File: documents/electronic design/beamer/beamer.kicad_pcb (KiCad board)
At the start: 2 copper layers, 23 parts, among them P1 CONN_01X20, P2 CONN_01X20, T1 2N7002K, T10 2N7002K, T2 2N7002K, T3 2N7002K, T4 2N7002K, T5 2N7002K, T6 2N7002K, T7 2N7002K, T8 2N7002K, T9 2N7002K, U1 NRF24L01-BRKOUT

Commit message: update pcb
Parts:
- moved U1 97.5 mm to (224.5, 110.7), turned to 270 degrees
- moved R1 91.4 mm to (172.7, 109.2), turned to 90 degrees
- moved P1 71.7 mm to (193.0, 124.5)
- moved P2 71.7 mm to (193.0, 109.2)
- moved D4 58.6 mm to (90.0, 110.1)
- moved D5 58.6 mm to (105.0, 110.1)
- moved D6 58.6 mm to (120.0, 110.1)
- moved D7 58.6 mm to (135.0, 110.1)
- moved D8 58.6 mm to (150.0, 110.1)
- moved D9 58.6 mm to (165.0, 110.1)
- moved D1 58.6 mm to (45.0, 110.1)
- moved D2 58.6 mm to (60.0, 110.1)
- moved D3 58.6 mm to (75.0, 110.1)
- moved T10 50.1 mm to (163.7, 114.3)
- moved T8 50.1 mm to (133.7, 114.3)
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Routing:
- net Net-(D1-Pad1): track 125.6 -> 4.52 mm
- net Net-(D2-Pad1): track 101.0 -> 4.52 mm
- net Net-(D5-Pad1): track 94.8 -> 4.52 mm
- net Net-(D4-Pad1): track 86.1 -> 4.52 mm
- net Net-(D3-Pad1): track 83.8 -> 4.52 mm
- net PWM_38K: track 74.3 -> 0.00 mm
- net IR_PIN_1: track 64.4 -> 0.00 mm
- net IR_PIN_ID: track 58.1 -> 0.00 mm
- net IR_PIN_2: track 51.4 -> 0.00 mm
- net IR_PIN_8: track 46.4 -> 0.00 mm
- net IR_PIN_3: track 38.5 -> 0.00 mm
- net GND: track 0.00 -> 37.1 mm
- net IR_PIN_7: track 34.0 -> 0.00 mm
- net +3V3: track 0.00 -> 31.6 mm
- net IR_PIN_4: track 27.7 -> 0.00 mm
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
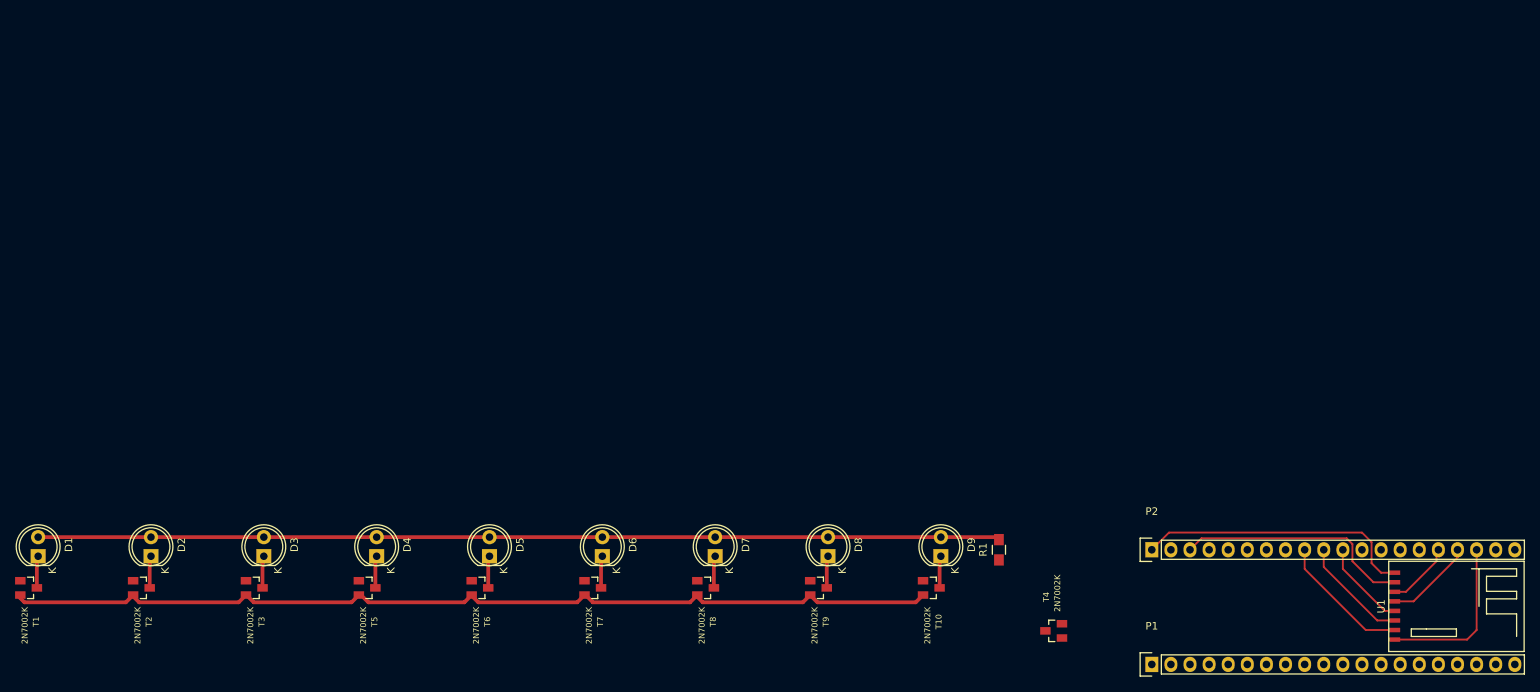
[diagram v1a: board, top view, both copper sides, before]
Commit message: finish pcb for beamer (prototype v1)
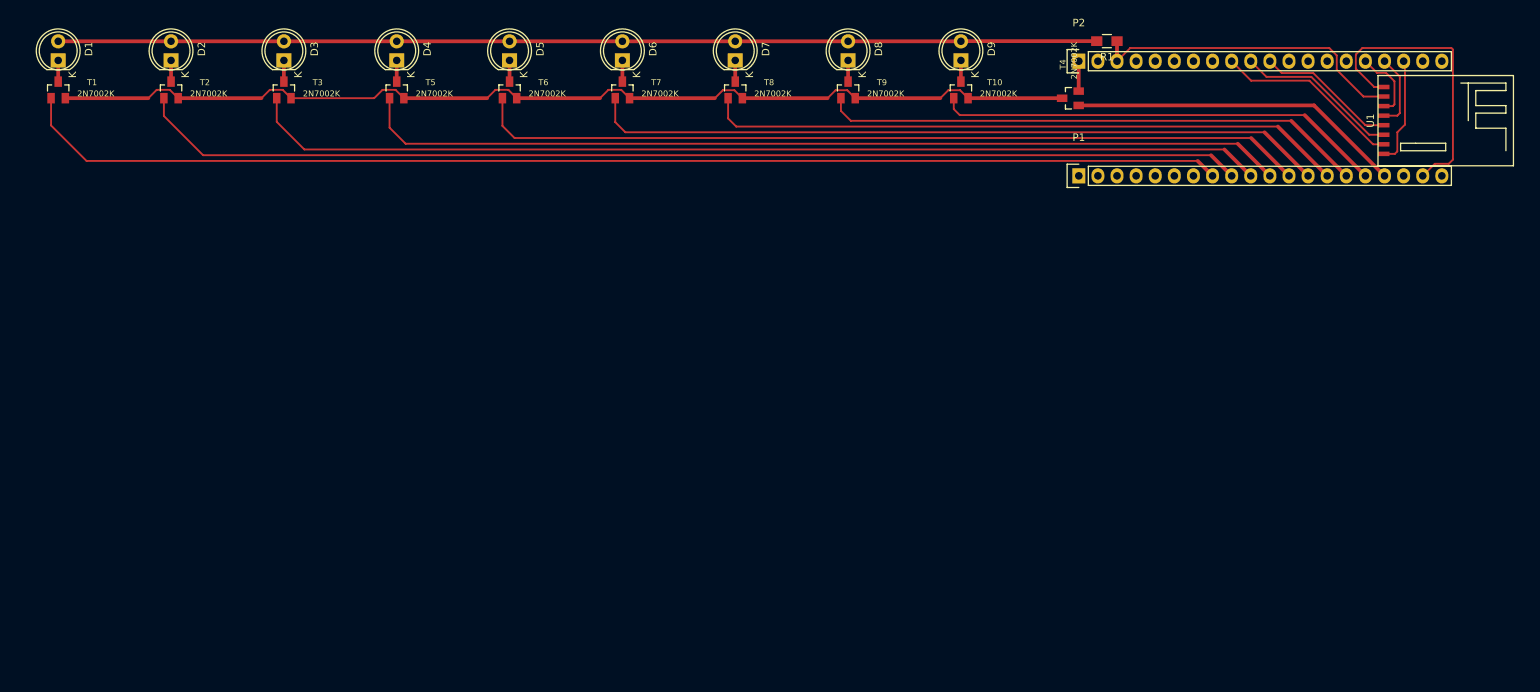
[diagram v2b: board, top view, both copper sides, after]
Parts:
- moved T4 70.8 mm to (182.2, 49.2)
- moved R1 69.1 mm to (187.1, 41.6), turned to 180 degrees
- moved T10 66.3 mm to (167.7, 48.1), turned to 0 degrees
- moved T8 66.3 mm to (137.7, 48.1), turned to 0 degrees
- moved T9 66.3 mm to (152.7, 48.1), turned to 0 degrees
- moved T1 66.3 mm to (47.7, 48.1), turned to 0 degrees
- moved T2 66.3 mm to (62.7, 48.1), turned to 0 degrees
- moved T3 66.3 mm to (77.7, 48.1), turned to 0 degrees
- moved T5 66.3 mm to (92.7, 48.1), turned to 0 degrees
- moved T6 66.3 mm to (107.7, 48.1), turned to 0 degrees
- moved T7 66.3 mm to (122.7, 48.1), turned to 0 degrees
- moved D1 66.0 mm to (47.7, 44.2)
- moved D2 66.0 mm to (62.7, 44.2)
- moved D3 66.0 mm to (77.7, 44.2)
- moved D4 66.0 mm to (92.7, 44.2)
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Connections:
- P1 pad 19: Net-(P1-Pad19) -> GND
- P1 pad 20: Net-(P1-Pad20) -> +3V3
- P2 pad 2: Net-(P2-Pad2) -> GND
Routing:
- net IR_PIN_1: track 0.00 -> 160.8 mm
- net IR_PIN_2: track 0.00 -> 147.6 mm
- net IR_PIN_3: track 0.00 -> 135.6 mm
- net IR_PIN_4: track 0.00 -> 123.6 mm
- net IR_PIN_5: track 0.00 -> 111.0 mm
- net IR_PIN_6: track 0.00 -> 98.2 mm
- net IR_PIN_7: track 0.00 -> 85.5 mm
- net IR_PIN_8: track 0.00 -> 72.4 mm
- net IR_PIN_ID: track 0.00 -> 59.8 mm
- net PWM_38K: track 0.00 -> 44.5 mm
- net Net-(T1-Pad2): track 127.0 -> 139.7 mm
- net +3V3: track 31.6 -> 42.7 mm
- net Net-(D1-Pad2): track 127.9 -> 138.1 mm
- net NRF_IRQ1: track 22.1 -> 14.4 mm
- net SPI1_MOSI: track 14.6 -> 21.7 mm
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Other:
- net class Default: trace_width 0.25 -> 0.5

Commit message: thick traces
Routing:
- net GND: track 43.5 -> 78.6 mm
- net IR_PIN_2: track 147.6 -> 158.9 mm
- net IR_PIN_3: track 135.6 -> 143.9 mm
- net +3V3: track 42.7 -> 50.2 mm
- net IR_PIN_1: track 160.8 -> 167.5 mm
- net IR_PIN_4: track 123.6 -> 126.6 mm
- net IR_PIN_5: track 111.0 -> 113.3 mm
- net IR_PIN_6: track 98.2 -> 100.1 mm
- net IR_PIN_8: track 72.4 -> 74.3 mm
- net IR_PIN_7: track 85.5 -> 87.0 mm
- net IR_PIN_ID: track 59.8 -> 61.0 mm

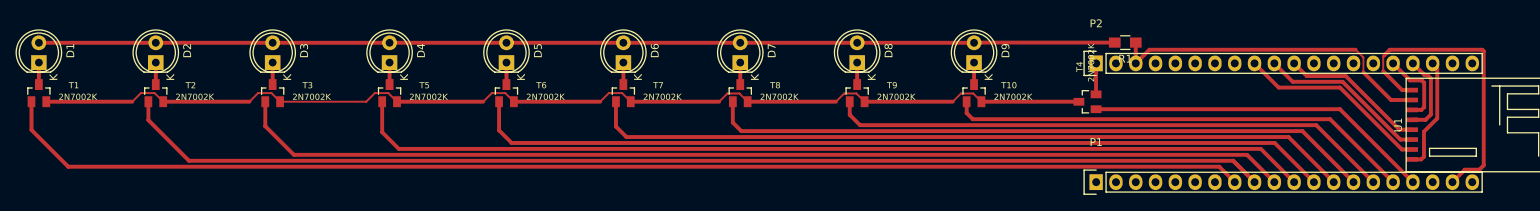
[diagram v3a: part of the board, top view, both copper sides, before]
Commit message: change pin numbers in transmitter routine; remake pcb
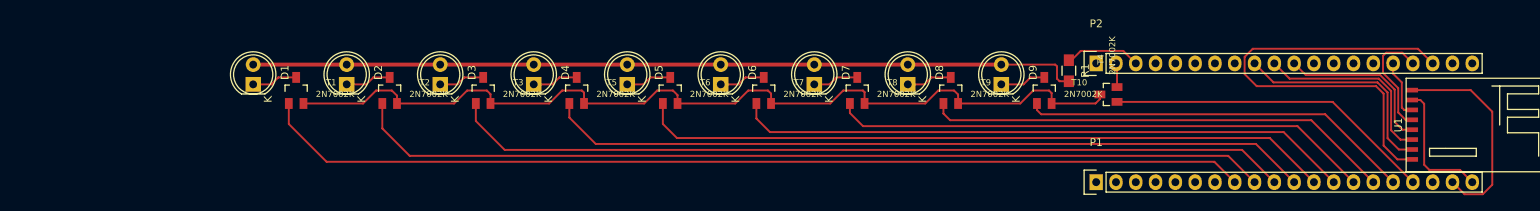
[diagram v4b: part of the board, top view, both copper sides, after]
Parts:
- T1, T10, T2, T3, T5, T6, T7, T8, T9: footprint 2N7002K:SOT23 -> sot23_modified:SOT23Mod
- moved T1 33.0 mm to (80.7, 47.7)
- moved T2 30.0 mm to (92.7, 47.7)
- moved D1 27.6 mm to (75.2, 47.0)
- moved T3 27.0 mm to (104.7, 47.7)
- moved D2 24.7 mm to (87.2, 47.0)
- moved T5 24.0 mm to (116.7, 47.7)
- moved D3 21.7 mm to (99.2, 47.0)
- moved T6 21.0 mm to (128.7, 47.7)
- moved D4 18.7 mm to (111.2, 47.0)
- moved T7 18.0 mm to (140.7, 47.7)
- moved D5 15.7 mm to (123.2, 47.0)
- moved T8 15.0 mm to (152.7, 47.7)
- moved D6 12.8 mm to (135.2, 47.0)
- moved T9 12.0 mm to (164.7, 47.7)
- moved D7 9.90 mm to (147.2, 47.0)
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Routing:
- net GND: track 78.6 -> 30.6 mm
- net NRF_IRQ1: track 14.8 -> 57.7 mm
- net IR_PIN_2: track 158.9 -> 118.0 mm
- net IR_PIN_1: track 167.5 -> 127.1 mm
- net IR_PIN_3: track 143.9 -> 108.0 mm
- net Net-(D1-Pad2): track 138.1 -> 107.7 mm
- net IR_PIN_4: track 126.6 -> 98.2 mm
- net IR_PIN_5: track 113.3 -> 89.3 mm
- net +3V3: track 50.2 -> 27.1 mm
- net IR_PIN_6: track 100.1 -> 79.4 mm
- net Net-(T1-Pad2): track 139.7 -> 119.8 mm
- net IR_PIN_7: track 87.0 -> 69.5 mm
- net IR_PIN_8: track 74.3 -> 60.1 mm
- net IR_PIN_ID: track 61.0 -> 50.4 mm
- net NRF_CSN1: track 10.4 -> 14.8 mm
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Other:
- net class Default: trace_width 0.5 -> 0.25

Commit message: add capacitor to pcb
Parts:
- added C1: C, Capacitors_SMD:C_1210_HandSoldering, F.Cu at (237.5, 44.2)
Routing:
- net +3V3: track 27.1 -> 61.3 mm
- net GND: track 30.6 -> 48.9 mm
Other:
- net class Default: trace_width 0.25 -> 0.5
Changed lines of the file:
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@@
 (kicad_pcb (version 4) (host pcbnew 4.0.2-stable)
   (general
-    (links 50)
+    (links 52)
     (no_connects 8)
-    (area 15.8222 13.9172 278.230001 189.330001)
+    (area 14.6792 16.7112 276.960001 190.3522)
     (thickness 1.6)
     (drawings 0)
-    (tracks 182)
+    (tracks 196)
     (zones 0)
-    (modules 23)
+    (modules 24)
     (nets 49)
   )
@@
     (35 F.Paste user)
     (36 B.SilkS user)
-    (37 F.SilkS user hide)
+    (37 F.SilkS user)
     (38 B.Mask user)
     (39 F.Mask user)
@@
   )
   (setup
-    (last_trace_width 0.25)
+    (last_trace_width 0.5)
     (trace_clearance 0.2)
     (zone_clearance 0.508)
@@
   (net_class Default "This is the default net class."
     (clearance 0.2)
-    (trace_width 0.25)
+    (trace_width 0.5)
     (via_dia 0.6)
     (via_drill 0.4)
@@
     (pad 3 smd rect (at 0.00254 -1.64338) (size 1 1.4) (layers F.Cu F.Paste F.Mask)
       (net 10 "Net-(D9-Pad1)") (solder_mask_margin 0.2))
+  )
+  (module Capacitors_SMD:C_1210_HandSoldering (layer F.Cu)
+    (at 237.49 44.196)
+    (descr "Capacitor SMD 1210, hand soldering")
+    (tags "capacitor 1210")
+    (attr smd)
+    (fp_text reference C1 (at 0 -2.7) (layer F.SilkS)
+      (effects (font (size 1 1) (thickness 0.15)))
+    )
+    (fp_text value C (at 0 2.7) (layer F.Fab)
+      (effects (font (size 1 1) (thickness 0.15)))
+    )
+    (fp_line (start -3.3 -1.6) (end 3.3 -1.6) (layer F.CrtYd) (width 0.05))
+    (fp_line (start -3.3 1.6) (end 3.3 1.6) (layer F.CrtYd) (width 0.05))
+    (fp_line (start -3.3 -1.6) (end -3.3 1.6) (layer F.CrtYd) (width 0.05))
+    (fp_line (start 3.3 -1.6) (end 3.3 1.6) (layer F.CrtYd) (width 0.05))
+    (fp_line (start 1 -1.475) (end -1 -1.475) (layer F.SilkS) (width 0.15))
+    (fp_line (start -1 1.475) (end 1 1.475) (layer F.SilkS) (width 0.15))
+    (pad 1 smd rect (at -2 0) (size 2 2.5) (layers F.Cu F.Paste F.Mask)
+      (net 26 GND))
+    (pad 2 smd rect (at 2 0) (size 2 2.5) (layers F.Cu F.Paste F.Mask)
+      (net 27 +3V3))
+    (model Capacitors_SMD.3dshapes/C_1210_HandSoldering.wrl
+      (at (xyz 0 0 0))
+      (scale (xyz 1 1 1))
+      (rotate (xyz 0 0 0))
+    )
   )
   (segment (start 75.1638 46.9652) (end 77.4948 46.9652) (width 0.25) (layer F.Cu) (net 1))
@@
   (segment (start 186.012 49.21) (end 213.675 49.21) (width 0.25) (layer F.Cu) (net 24))
   (segment (start 213.675 49.21) (end 223.9772 59.5122) (width 0.25) (layer F.Cu) (net 24))
+  (segment (start 235.49 44.196) (end 234.8992 44.196) (width 0.5) (layer F.Cu) (net 26))
+  (segment (start 234.8992 44.196) (end 231.394 47.7012) (width 0.5) (layer F.Cu) (net 26))
+  (segment (start 223.8756 47.7012) (end 231.394 47.7012) (width 0.5) (layer F.Cu) (net 26))
+  (segment (start 231.394 47.7012) (end 233.68 49.9872) (width 0.5) (layer F.Cu) (net 26))
+  (segment (start 233.68 49.9872) (end 233.68 57.15) (width 0.5) (layer F.Cu) (net 26))
+  (segment (start 233.68 57.15) (end 232.918 57.912) (width 0.5) (layer F.Cu) (net 26))
+  (segment (start 232.918 57.912) (end 230.378 57.912) (width 0.5) (layer F.Cu) (net 26))
+  (segment (start 230.378 57.912) (end 229.0572 59.2328) (width 0.5) (layer F.Cu) (net 26))
+  (segment (start 229.0572 59.2328) (end 229.0572 59.5122) (width 0.5) (layer F.Cu) (net 26))
+  (segment (start 229.0572 59.5122) (end 229.0572 59.2328) (width 0.25) (layer F.Cu) (net 26))
+  (segment (start 229.0572 59.2328) (end 230.378 57.912) (width 0.25) (layer F.Cu) (net 26))
+  (segment (start 230.378 57.912) (end 232.918 57.912) (width 0.25) (layer F.Cu) (net 26))
+  (segment (start 232.918 57.912) (end 233.68 57.15) (width 0.25) (layer F.Cu) (net 26))
+  (segment (start 233.68 57.15) (end 233.68 49.9872) (width 0.25) (layer F.Cu) (net 26))
+  (segment (start 233.68 49.9872) (end 231.394 47.7012) (width 0.25) (layer F.Cu) (net 26))
   (segment (start 186.012 47.31) (end 186.012 44.407) (width 0.25) (layer F.Cu) (net 26))
   (segment (start 186.012 44.407) (end 185.8772 44.2722) (width 0.25) (layer F.Cu) (net 26))
   (segment (start 183.0148 44.5946) (end 183.3372 44.2722) (width 0.25) (layer F.Cu) (net 26))
-  (segment (start 223.8756 47.7012) (end 231.394 47.7012) (width 0.25) (layer F.Cu) (net 26))
-  (segment (start 230.6066 61.0616) (end 229.0572 59.5122) (width 0.25) (layer F.Cu) (net 26))
-  (segment (start 232.9434 61.0616) (end 230.6066 61.0616) (width 0.25) (layer F.Cu) (net 26))
-  (segment (start 234.1626 59.8424) (end 232.9434 61.0616) (width 0.25) (layer F.Cu) (net 26))
-  (segment (start 234.1626 50.4698) (end 234.1626 59.8424) (width 0.25) (layer F.Cu) (net 26))
-  (segment (start 231.394 47.7012) (end 234.1626 50.4698) (width 0.25) (layer F.Cu) (net 26))
+  (segment (start 239.49 44.196) (end 239.49 59.0362) (width 0.5) (layer F.Cu) (net 27))
+  (segment (start 239.49 59.0362) (end 239.014 59.5122) (width 0.5) (layer F.Cu) (net 27))
+  (segment (start 239.014 59.5122) (end 231.5972 59.5122) (width 0.5) (layer F.Cu) (net 27))
+  (segment (start 239.014 59.5122) (end 231.5972 59.5122) (width 0.25) (layer F.Cu) (net 27))
+  (segment (start 239.49 59.0362) (end 239.014 59.5122) (width 0.25) (layer F.Cu) (net 27))
+  (segment (start 223.8756 48.9712) (end 224.9932 48.9712) (width 0.25) (layer F.Cu) (net 27))
+  (segment (start 230.0732 61.0362) (end 231.5972 59.5122) (width 0.25) (layer F.Cu) (net 27))
+  (segment (start 225.933 61.0362) (end 230.0732 61.0362) (width 0.25) (layer F.Cu) (net 27))
+  (segment (start 225.2472 60.3504) (end 225.933 61.0362) (width 0.25) (layer F.Cu) (net 27))
+  (segment (start 225.2472 49.2252) (end 225.2472 60.3504) (width 0.25) (layer F.Cu) (net 27))
+  (segment (start 224.9932 48.9712) (end 225.2472 49.2252) (width 0.25) (layer F.Cu) (net 27))
   (segment (start 179.832 43.862) (end 180.166 43.862) (width 0.25) (layer F.Cu) (net 27))
   (segment (start 180.166 43.862) (end 181.356 42.672) (width 0.25) (layer F.Cu) (net 27))
   (segment (start 181.356 42.672) (end 186.817 42.672) (width 0.25) (layer F.Cu) (net 27))
   (segment (start 186.817 42.672) (end 188.4172 44.2722) (width 0.25) (layer F.Cu) (net 27))
-  (segment (start 223.8756 48.9712) (end 224.9424 48.9712) (width 0.25) (layer F.Cu) (net 27))
-  (segment (start 230.0224 57.9374) (end 231.5972 59.5122) (width 0.25) (layer F.Cu) (net 27))
-  (segment (start 226.0854 57.9374) (end 230.0224 57.9374) (width 0.25) (layer F.Cu) (net 27))
-  (segment (start 225.425 57.277) (end 226.0854 57.9374) (width 0.25) (layer F.Cu) (net 27))
-  (segment (start 225.425 49.4538) (end 225.425 57.277) (width 0.25) (layer F.Cu) (net 27))
-  (segment (start 224.9424 48.9712) (end 225.425 49.4538) (width 0.25) (layer F.Cu) (net 27))
   (segment (start 223.8756 48.9712) (end 224.536 48.9712) (width 0.25) (layer F.Cu) (net 27))
+  (segment (start 95.25 56.134) (end 200.279 56.134) (width 0.25) (layer F.Cu) (net 31))
+  (segment (start 91.7358 52.6198) (end 95.25 56.134) (width 0.25) (layer F.Cu) (net 31))
   (segment (start 91.7358 49.41834) (end 91.7358 52.6198) (width 0.25) (layer F.Cu) (net 31))
   (segment (start 200.279 56.134) (end 203.6572 59.5122) (width 0.25) (layer F.Cu) (net 31))
-  (segment (start 95.25 56.134) (end 200.279 56.134) (width 0.25) (layer F.Cu) (net 31))
-  (segment (start 91.7358 52.6198) (end 95.25 56.134) (width 0.25) (layer F.Cu) (net 31))
   (segment (start 79.7358 49.41834) (end 79.7358 52.0498) (width 0.25) (layer F.Cu) (net 32))
   (segment (start 198.501 56.896) (end 201.1172 59.5122) (width 0.25) (layer F.Cu) (net 32))

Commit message: update pcb for beamer
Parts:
- moved D6 1.61 mm to (134.7, 45.4)
- moved D7 1.61 mm to (146.7, 45.4)
- moved D8 1.61 mm to (158.7, 45.4)
- moved D9 1.61 mm to (170.7, 45.4)
- moved T1 1.61 mm to (80.2, 46.2)
- moved T10 1.61 mm to (176.2, 46.2)
- moved T2 1.61 mm to (92.2, 46.2)
- moved T3 1.61 mm to (104.2, 46.2)
- moved T5 1.61 mm to (116.2, 46.2)
- moved T6 1.61 mm to (128.2, 46.2)
- moved T7 1.61 mm to (140.2, 46.2)
- moved T8 1.61 mm to (152.2, 46.2)
- moved T9 1.61 mm to (164.2, 46.2)
- moved D1 1.61 mm to (74.7, 45.4)
- moved D2 1.61 mm to (86.7, 45.4)
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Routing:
- net Net-(D1-Pad2): track 107.7 -> 180.9 mm
- net IR_PIN_4: track 98.2 -> 102.0 mm
- net IR_PIN_6: track 79.4 -> 83.1 mm
- net IR_PIN_7: track 69.5 -> 73.1 mm
- net IR_PIN_5: track 89.3 -> 92.6 mm
- net +3V3: track 61.3 -> 64.6 mm
- net Net-(D9-Pad1): track 5.88 -> 8.92 mm
- net IR_PIN_3: track 108.0 -> 110.8 mm
- net IR_PIN_8: track 60.1 -> 62.9 mm
- net IR_PIN_ID: track 50.4 -> 52.8 mm
- net SPI1_MISO: track 28.2 -> 26.1 mm
- net NRF_IRQ1: track 57.7 -> 55.6 mm
- net IR_PIN_1: track 127.1 -> 129.1 mm
- net IR_PIN_2: track 118.0 -> 119.9 mm
- net SPI1_MOSI: track 24.7 -> 22.8 mm
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
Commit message: updatebeamer schematic
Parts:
- added U2: 74HC595D, SOIC127P1030X265-16N:SOIC127P1030X265-16N, F.Cu at (71.8, 52.3)
- moved C1 229.4 mm to (8.36, 54.5), turned to 90 degrees
- moved U1 195.1 mm to (28.4, 58.0), turned to 90 degrees
- moved P2 123.9 mm to (60.4, 59.6), turned to 180 degrees
- moved P1 123.8 mm to (60.4, 44.4), turned to 180 degrees
- moved T4 4.69 mm to (180.3, 46.8), turned to 0 degrees
- moved R1 2.34 mm to (177.6, 42.1), turned to 180 degrees
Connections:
- P1 pad 10: IR_PIN_3 -> Net-(P1-Pad10)
- P1 pad 11: IR_PIN_4 -> Net-(P1-Pad11)
- P1 pad 12: IR_PIN_5 -> Net-(P1-Pad12)
- P1 pad 13: IR_PIN_6 -> Net-(P1-Pad13)
- P1 pad 14: IR_PIN_7 -> Net-(P1-Pad14)
- P1 pad 15: IR_PIN_8 -> Net-(P1-Pad15)
- P1 pad 8: IR_PIN_1 -> Net-(P1-Pad8)
- P1 pad 9: IR_PIN_2 -> Net-(P1-Pad9)
- P2 pad 12: Net-(P2-Pad12) -> NRF_CSN1
- P2 pad 13: Net-(P2-Pad13) -> NRF_CE1
- P2 pad 14: Net-(P2-Pad14) -> ShiftReg_Expose
- P2 pad 16: NRF_CE1 -> Net-(P2-Pad16)
- P2 pad 17: NRF_CSN1 -> Net-(P2-Pad17)
- P2 pad 18: NRF_IRQ1 -> Net-(P2-Pad18)
- P2 pad 8: Net-(P2-Pad8) -> NRF_IRQ1
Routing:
- net IR_PIN_1: track 129.1 -> 3.92 mm
- net IR_PIN_2: track 119.9 -> 16.7 mm
- net IR_PIN_3: track 110.8 -> 29.9 mm
- net IR_PIN_4: track 102.0 -> 43.1 mm
- net IR_PIN_ID: track 52.8 -> 0.00 mm
- net PWM_38K: track 43.4 -> 0.00 mm
- net IR_PIN_8: track 62.9 -> 106.0 mm
- net IR_PIN_5: track 92.6 -> 56.3 mm
- net +3V3: track 64.6 -> 30.1 mm
- net NRF_IRQ1: track 55.6 -> 21.3 mm
- net IR_PIN_6: track 83.1 -> 69.7 mm
- net IR_PIN_7: track 73.1 -> 82.7 mm
- net Net-(D1-Pad2): track 180.9 -> 172.5 mm
- net SPI1_MISO: track 26.1 -> 18.3 mm
- net SPI1_MOSI: track 22.8 -> 15.4 mm
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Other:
- net class Default: clearance 0.2 -> 0.3
- rule trace_clearance: 0.2 -> 0.3
